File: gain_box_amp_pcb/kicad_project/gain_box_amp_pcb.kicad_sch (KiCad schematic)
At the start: 58 parts, among them J1 Conn_01x02, J2 Conn_01x02, J3 Conn_01x02, J4 Conn_01x02, J5 Conn_01x02, J6 Conn_01x02, J7 Conn_01x02, J8 Conn_01x03, J9 Conn_01x04, K1 J104D2C12VDC.36S, K2 J104D2C12VDC.36S, K3 G5V-1, U1 NE5532, U2 NE5532, U3 NE5532, U4 140817141310

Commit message: Fix routing error
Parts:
- K3: value G5V-1 -> J104D2C12VDC.36S

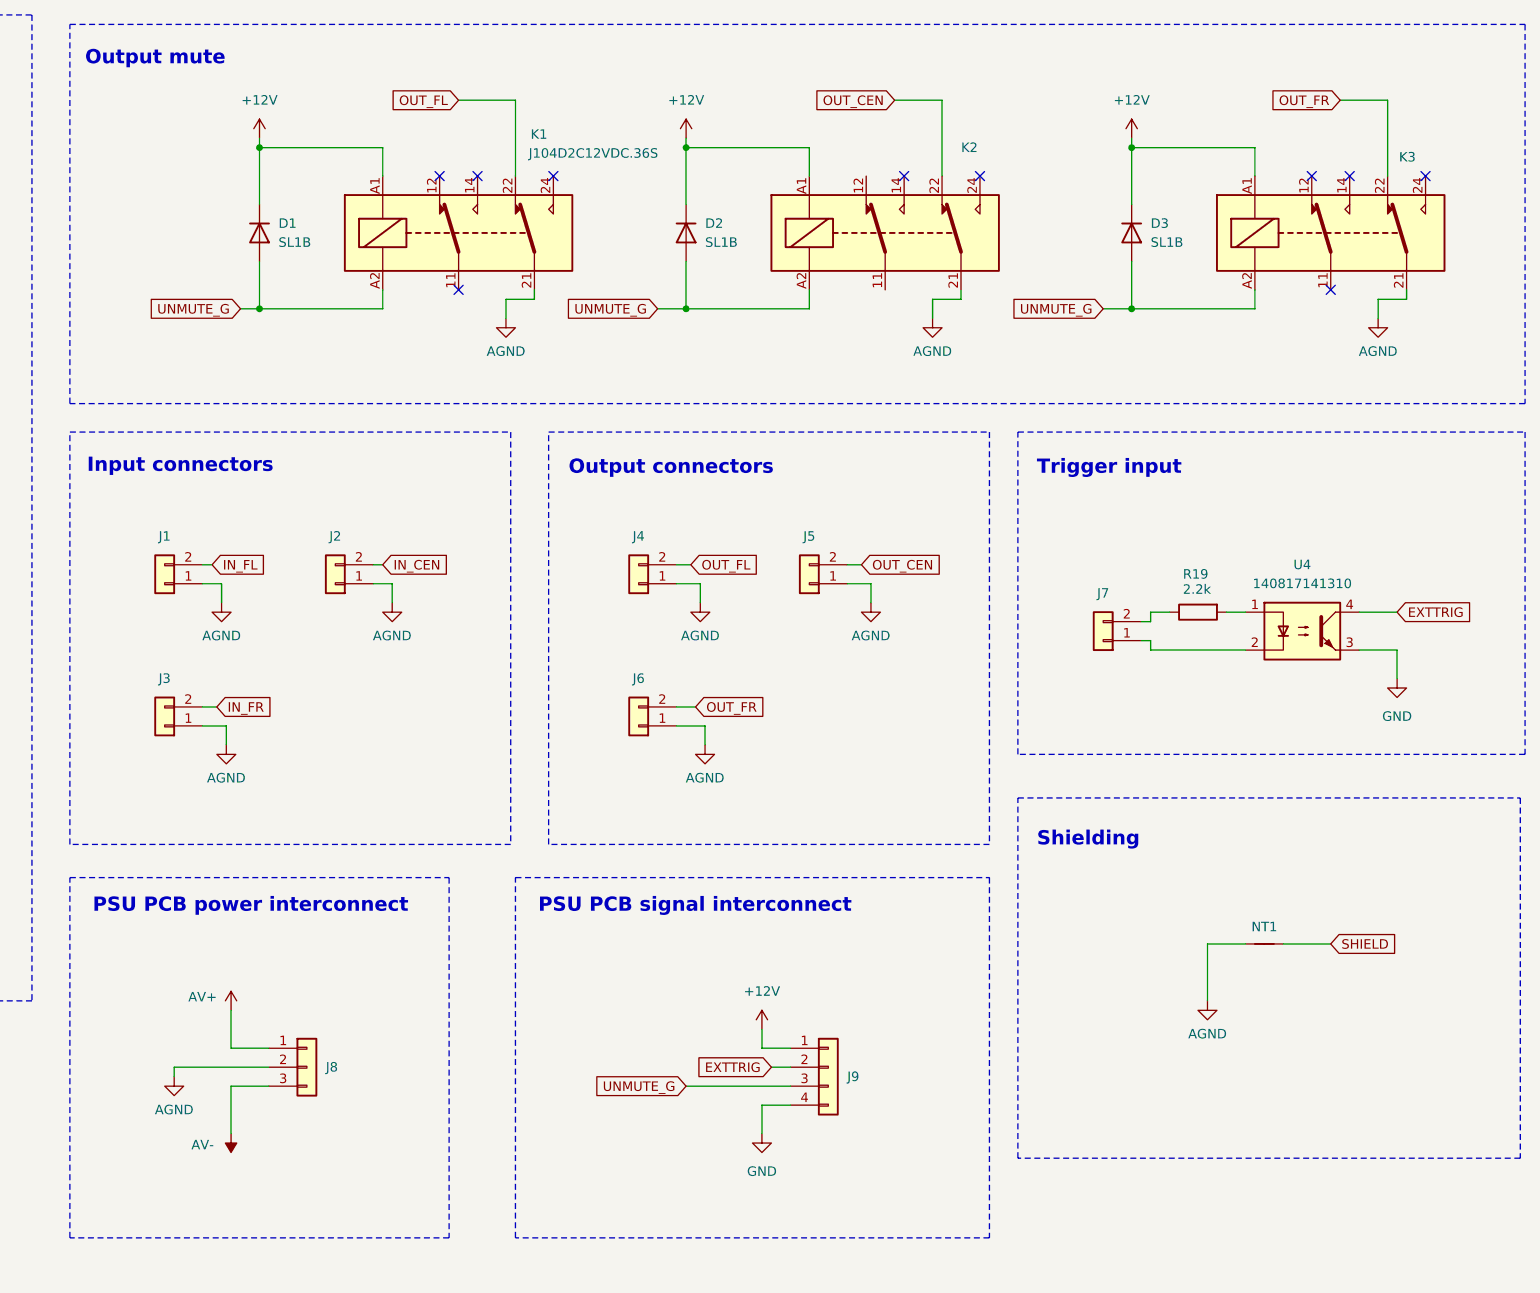
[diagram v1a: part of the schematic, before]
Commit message: Route new amp board
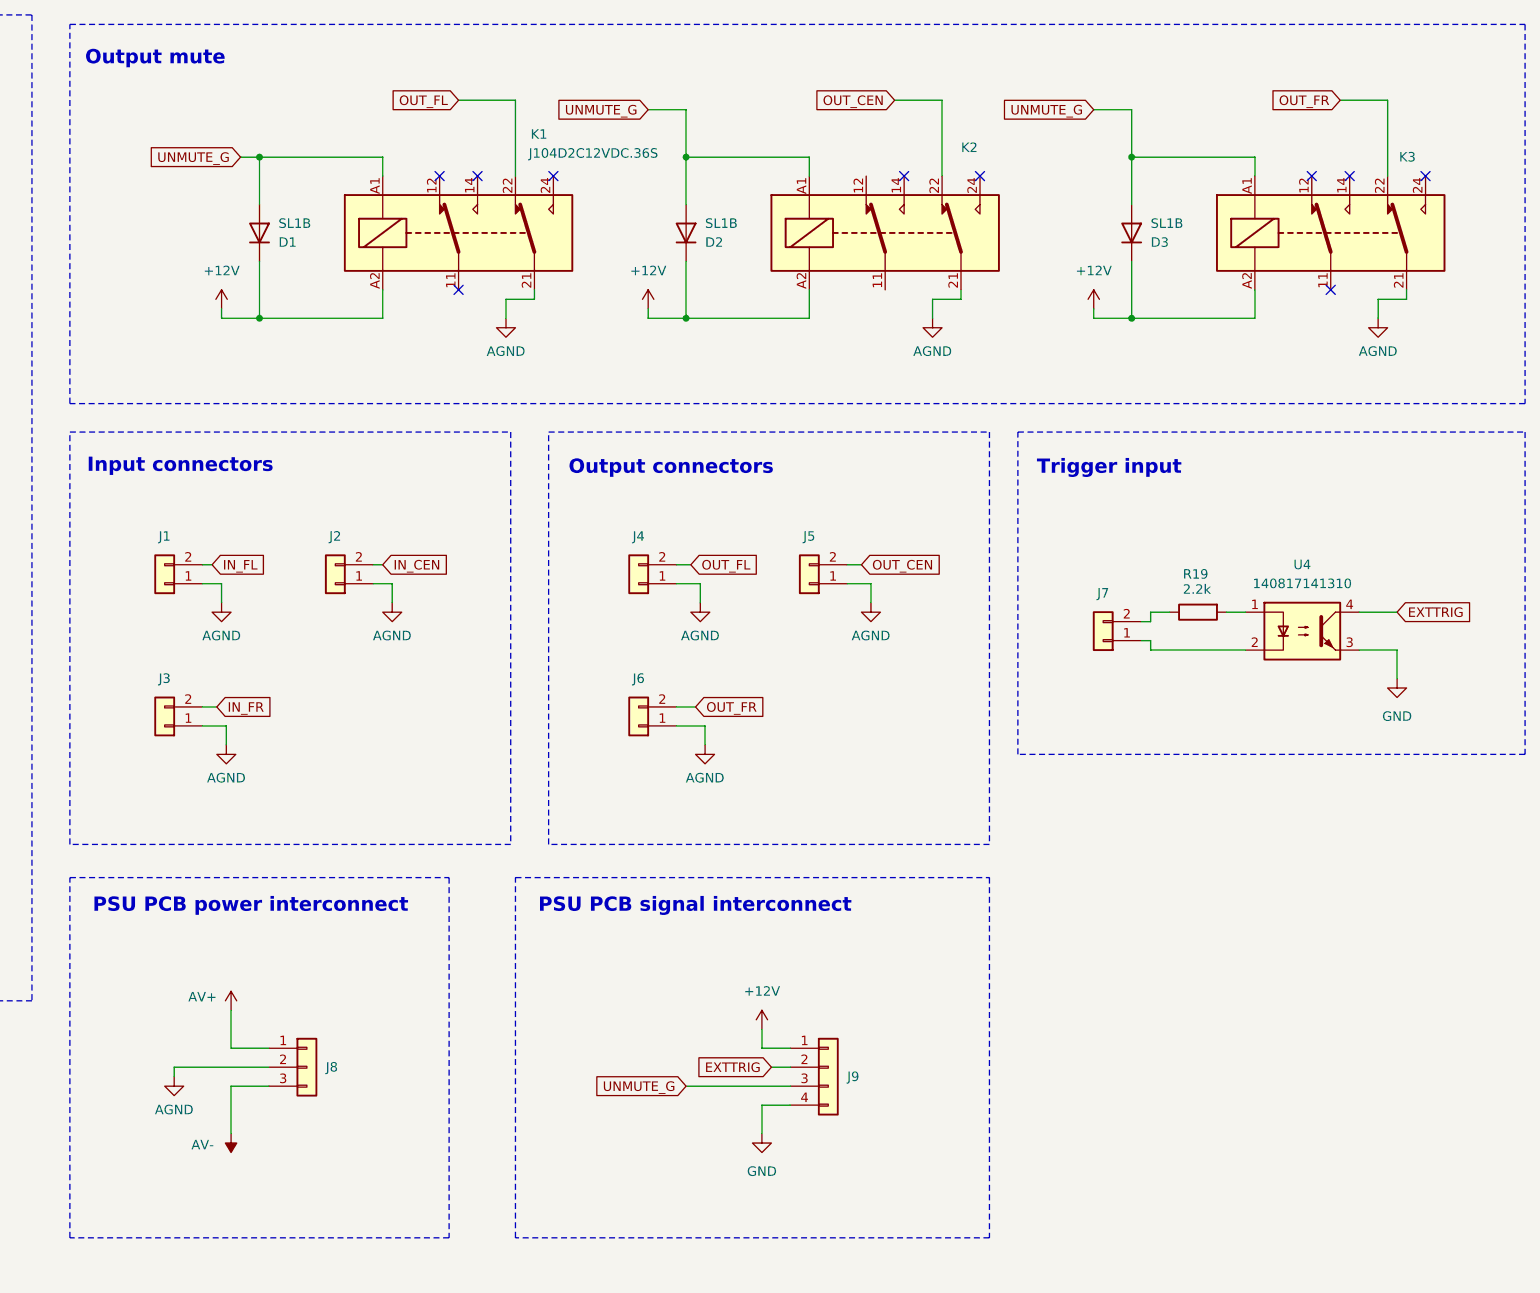
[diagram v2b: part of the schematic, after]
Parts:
- removed NT1: NetTie_2, NetTie:NetTie-2_THT_Pad1.0mm, symbol Device:NetTie_2
- C1, C2, C3: footprint Capacitor_THT:C_Rect_L7.2mm_W4.5mm_P5.00mm_FKS2_FKP2_MKS2_MKP2 -> Capacitor_THT:C_Rect_L18.0mm_W11.0mm_P15.00mm_FKS3_FKP3
- C4, C5, C6: footprint Capacitor_THT:C_Rect_L7.2mm_W2.5mm_P5.00mm_FKS2_FKP2_MKS2_MKP2 -> Capacitor_THT:C_Rect_L13.0mm_W5.0mm_P10.00mm_FKS3_FKP3_MKS4
- C7, C8, C9: footprint Capacitor_THT:C_Rect_L13.0mm_W6.0mm_P10.00mm_FKS3_FKP3_MKS4 -> project_lib:C_Rect_L31.5mm_W12.5mm_P27.50mm_MKS4
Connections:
- net +12V: now also K1.A2, K2.A2, K3.A2; no longer K1.A1, K2.A1, K3.A1
- net UNMUTE_G: now also K1.A1, K2.A1, K3.A1; no longer K1.A2, K2.A2, K3.A2
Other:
- note removed: "Shielding"
